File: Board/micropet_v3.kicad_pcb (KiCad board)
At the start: 2 copper layers, 190.2 x 100.3 mm, 204 parts, among them CN3 PORT_CASSETTE_EDGE, CN4 PORT_IEEE_EDGE, IC1 512k x8 10ns SRAM, IC10 PIAPLCC, IC11 PIAPLCC, IC13 512k x8 10ns SRAM, IC16 74LVC8T245SO24, IC2 74245DW, IC3 7400D, IC4 7486D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

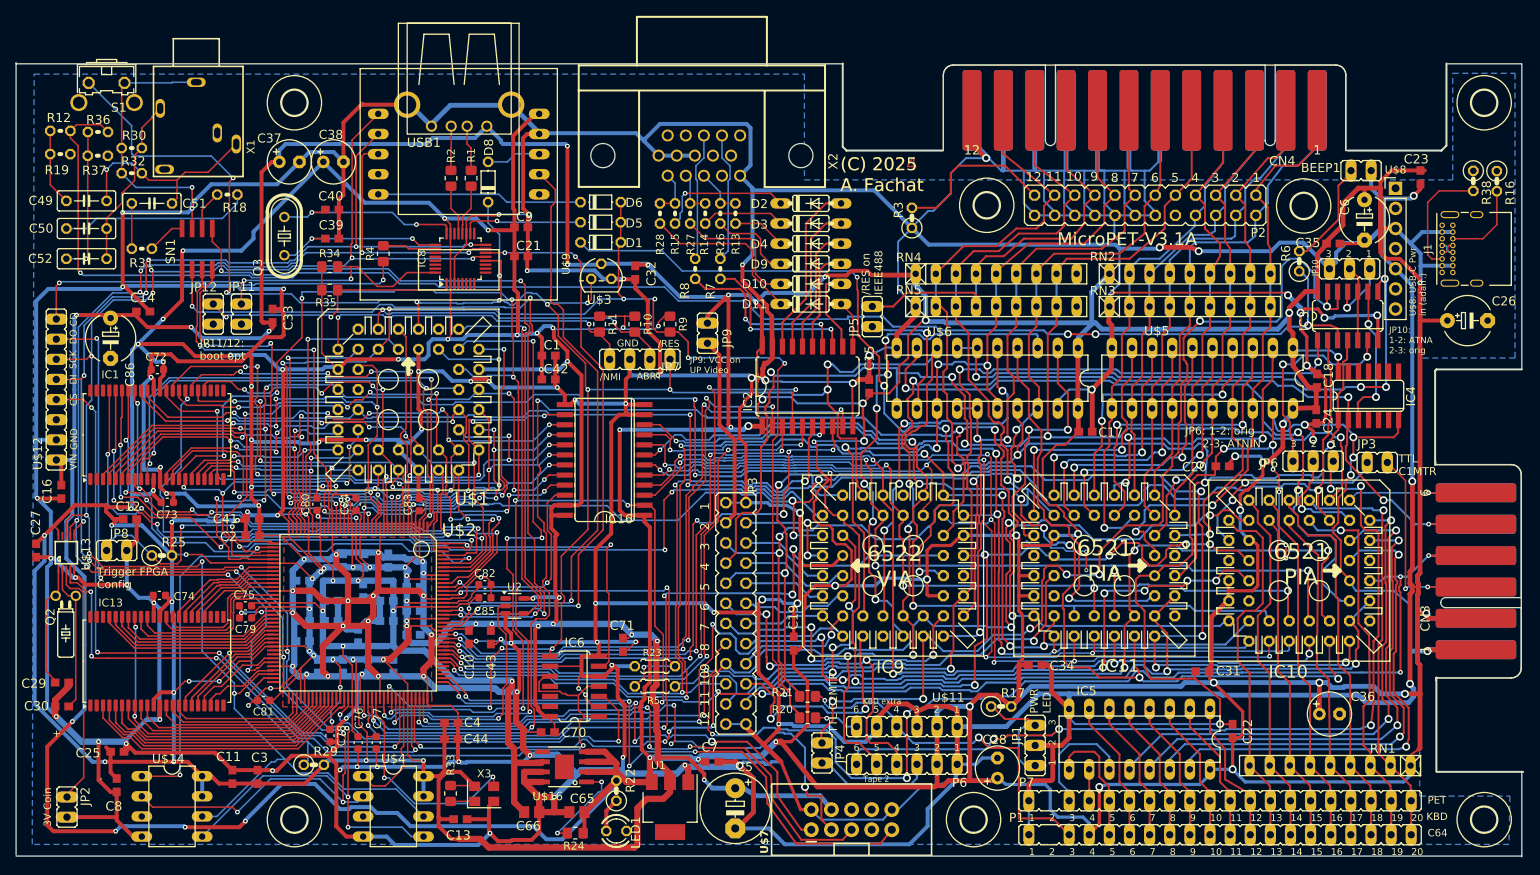
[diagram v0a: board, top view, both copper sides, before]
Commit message: final touches, 22u audio output caps
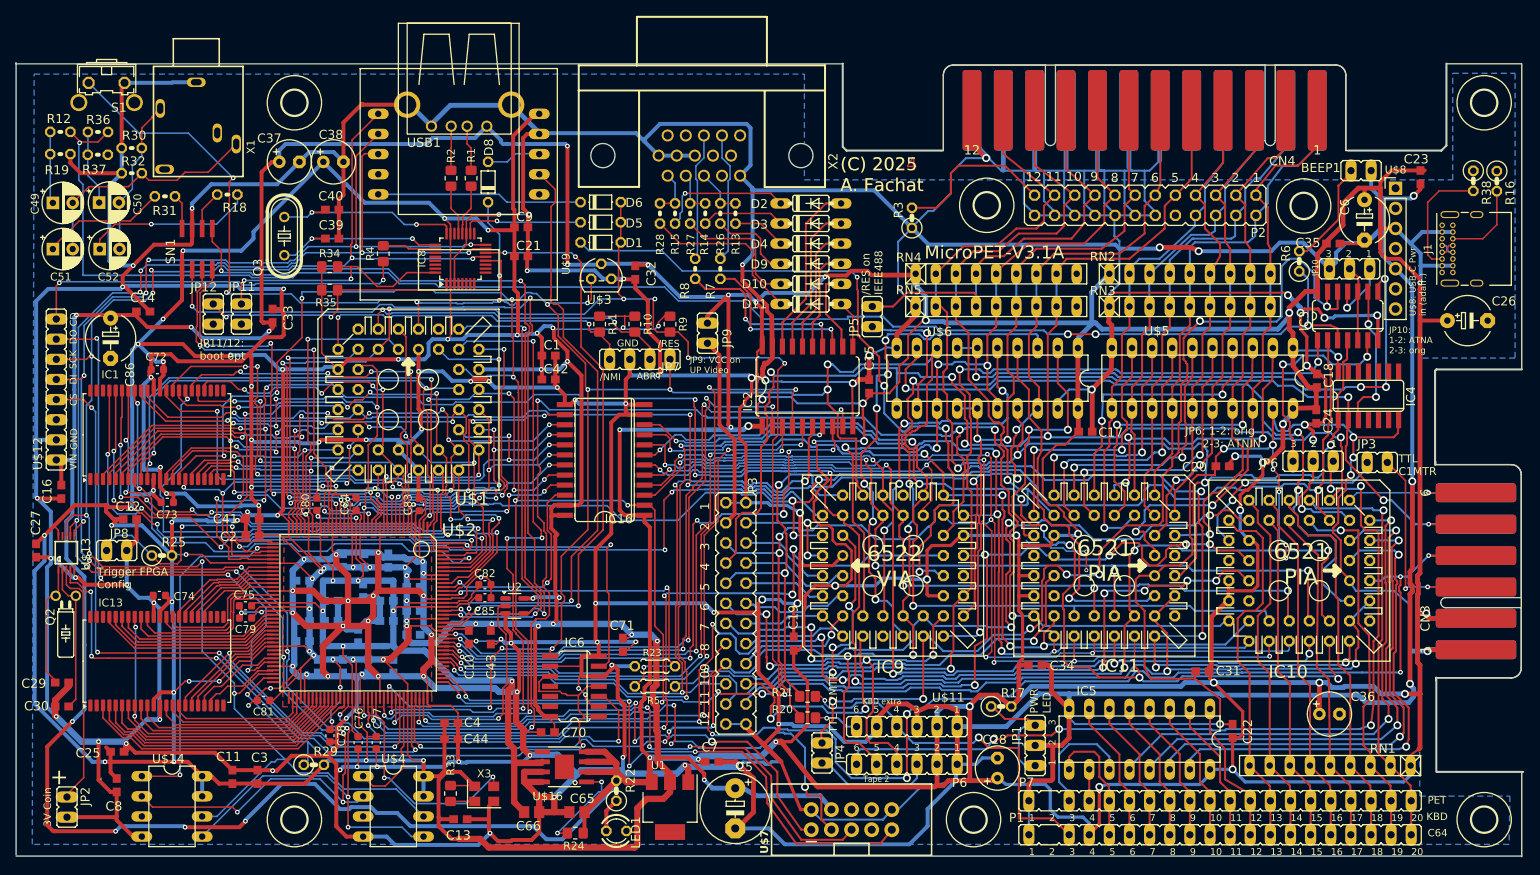
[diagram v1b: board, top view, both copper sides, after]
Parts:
- C49, C50, C51, C52: value 1u -> 22u; footprint micropet_v3:C050-025X075 -> Capacitor_THT:CP_Radial_D5.0mm_P2.50mm
- moved C51 13.8 mm to (78.3, 62.3)
- moved R31 7.22 mm to (92.5, 55.6)
- moved C49 4.25 mm to (78.3, 56.5)
- moved C50 3.65 mm to (84.2, 56.4)
- moved C52 2.07 mm to (84.2, 62.3)
- moved R37 0.13 mm to (84.0, 50.4)
- moved R12 0.13 mm to (79.2, 47.5)
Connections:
- R18 pad 2: Net-(C50-Pad1) -> Net-(C52-Pad1)
- R36 pad 1: Net-(C52-Pad1) -> Net-(C50-Pad1)
- R37 pad 1: Net-(C52-Pad1) -> Net-(C50-Pad1)
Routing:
- net Net-(C50-Pad1): track 24.0 -> 9.52 mm
- net Net-(C51-Pad1): track 5.71 -> 15.8 mm
- net GND: track 2155.5 -> 2161.7 mm, vias 120 -> 119
- net Net-(C49-Pad2): track 26.6 -> 30.3 mm, vias 1 -> 0
- net Net-(C52-Pad1): track 18.6 -> 21.6 mm
- net /RES: track 366.4 -> 364.3 mm
- net Net-(C50-Pad2): track 21.8 -> 19.9 mm
- net TTLSOUND: track 196.1 -> 194.6 mm
- net Net-(C49-Pad1): track 9.68 -> 9.10 mm
